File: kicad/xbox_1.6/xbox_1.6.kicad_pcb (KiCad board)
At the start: 4 copper layers, 210 parts, among them J1G1 jst_phd_12, J7G1 jst_phd_12, J8C1 IDC_40_Pin, Q3F1 SOT-23, U2C1 intel_495_bga2, U4B1 ddr_100_tqfp, U4C1 nvidia_xgpu_nv2a, U5F1 ddr_100_tqfp, U6D1 ddr_100_tqfp, U6E1 nvidia_mcpx

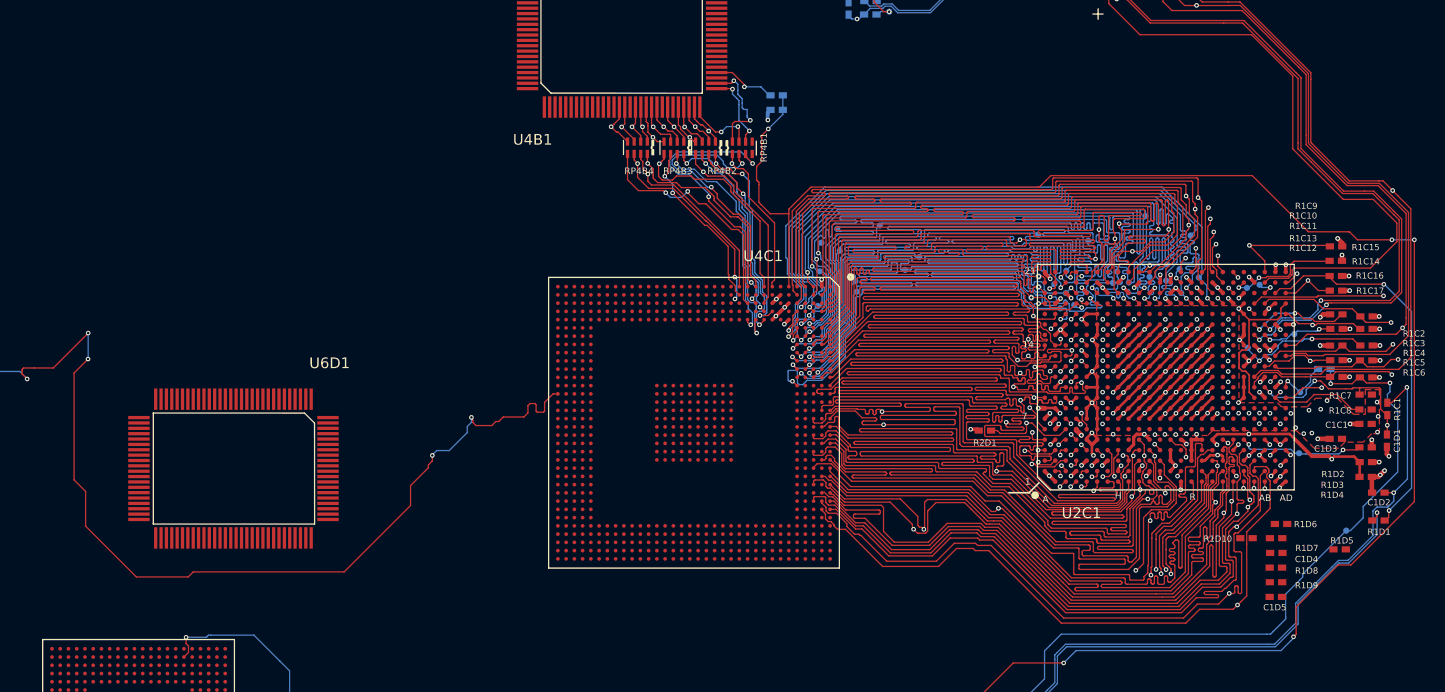
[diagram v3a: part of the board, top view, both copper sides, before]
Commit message: route more cpu signals
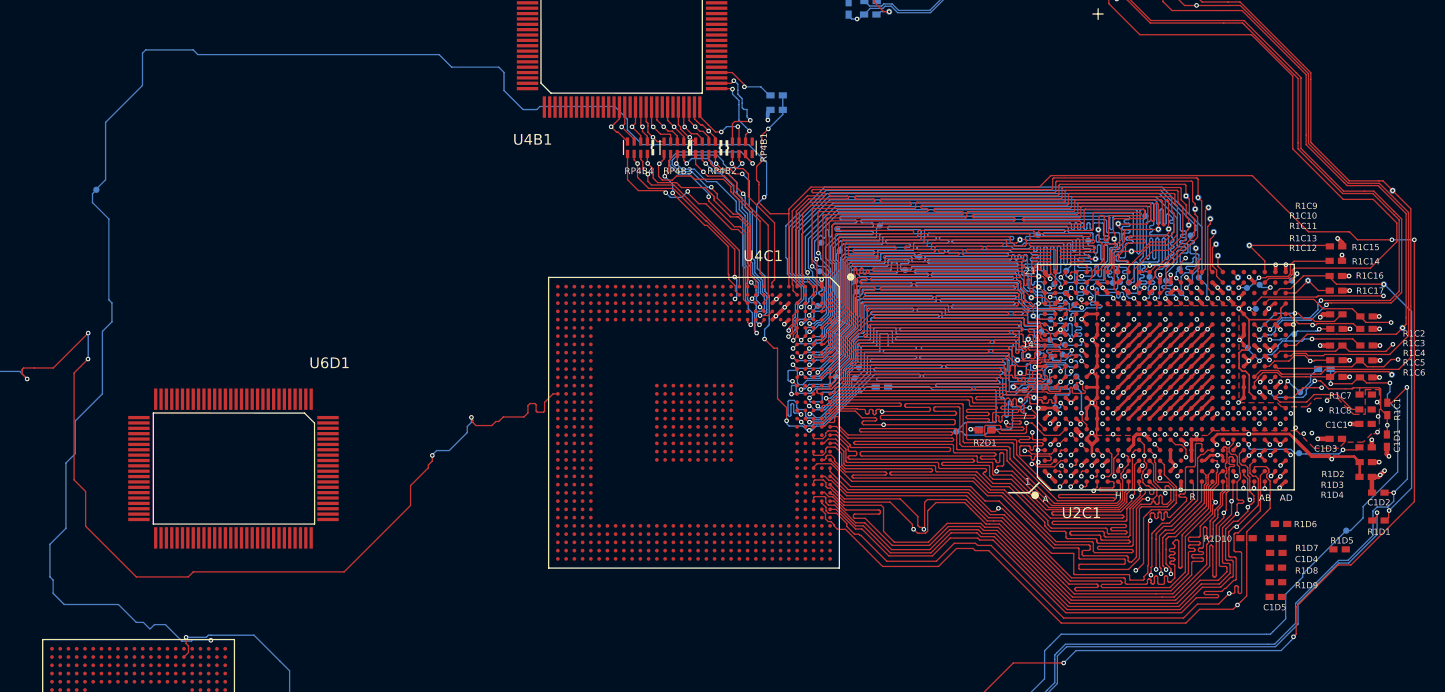
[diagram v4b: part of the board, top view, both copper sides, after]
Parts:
- added C2R8: 0603_smd, xbox_footprint:0603_smd, B.Cu at (253.3, 123.1)
- added R3P1: 0603_smd, xbox_footprint:0603_smd, B.Cu at (240.8, 118.0)
- added REF**: TP, xbox_footprint:TP, B.Cu at (301.6, 105.5)
- added REF**: TP, xbox_footprint:TP, B.Cu at (281.5, 102.1)
- added REF**: TP, xbox_footprint:TP, B.Cu at (278.8, 96.4)
- added REF**: TP, xbox_footprint:TP, B.Cu at (261.1, 117.3)
- added REF**: TP, xbox_footprint:TP, B.Cu at (274.3, 98.9)
- added REF**: TP, xbox_footprint:TP, B.Cu at (286.1, 108.5)
- added REF**: TP, xbox_footprint:TP, B.Cu at (280.6, 97.6)
- added REF**: TP, xbox_footprint:TP, B.Cu at (257.6, 116.3)
- added REF**: TP, xbox_footprint:TP, B.Cu at (285.3, 100.8)
- added REF**: TP, xbox_footprint:TP, B.Cu at (278.8, 101.2)
- added REF**: TP, xbox_footprint:TP, B.Cu at (284.0, 104.7)
- added REF**: TP, xbox_footprint:TP, B.Cu at (262.7, 114.0)
- added REF**: TP, xbox_footprint:TP, B.Cu at (302.6, 116.5)
- added REF**: TP, xbox_footprint:TP, B.Cu at (277.7, 94.8)
- added REF**: TP, xbox_footprint:TP, B.Cu at (257.5, 100.1)
- added REF**: TP, xbox_footprint:TP, B.Cu at (258.5, 112.2)
- added REF**: TP, xbox_footprint:TP, B.Cu at (290.5, 105.1)
- added REF**: TP, xbox_footprint:TP, B.Cu at (268.9, 100.0)
- added REF**: TP, xbox_footprint:TP, B.Cu at (261.8, 120.5)
- added REF**: TP, xbox_footprint:TP, B.Cu at (257.6, 119.6)
- added REF**: TP, xbox_footprint:TP, B.Cu at (257.2, 114.7)
- added REF**: TP, xbox_footprint:TP, B.Cu at (259.8, 113.9)
- added REF**: TP, xbox_footprint:TP, B.Cu at (278.0, 98.4)
- added REF**: TP, xbox_footprint:TP, B.Cu at (303.9, 110.8)
- added REF**: TP, xbox_footprint:TP, B.Cu at (280.4, 96.2)
- added REF**: TP, xbox_footprint:TP, B.Cu at (238.0, 115.6)
- added REF**: TP, xbox_footprint:TP, B.Cu at (260.1, 111.3)
- added REF**: TP, xbox_footprint:TP, B.Cu at (259.1, 109.4)
- added REF**: TP, xbox_footprint:TP, B.Cu at (264.3, 118.0)
- added REF**: TP, xbox_footprint:TP, B.Cu at (261.2, 109.8)
- added REF**: TP, xbox_footprint:TP, B.Cu at (237.5, 116.9)
- added REF**: TP, xbox_footprint:TP, B.Cu at (261.4, 114.3)
- added REF**: TP, xbox_footprint:TP, B.Cu at (249.8, 123.4)
- added REF**: TP, xbox_footprint:TP, B.Cu at (263.0, 112.9)
- added REF**: TP, xbox_footprint:TP, B.Cu at (275.6, 98.8)
- added REF**: TP, xbox_footprint:TP, B.Cu at (281.3, 100.7)
- added REF**: TP, xbox_footprint:TP, B.Cu at (258.5, 114.2)
- added REF**: TP, xbox_footprint:TP, B.Cu at (292.4, 105.1)
- added REF**: TP, xbox_footprint:TP, B.Cu at (258.1, 118.4)
- added REF**: TP, xbox_footprint:TP, B.Cu at (266.7, 102.5)
- added REF**: TP, xbox_footprint:TP, B.Cu at (279.1, 95.0)
- added REF**: TP, xbox_footprint:TP, B.Cu at (271.1, 101.5)
- added REF**: TP, xbox_footprint:TP, B.Cu at (145.6, 94.1)
- added REF**: TP, xbox_footprint:TP, B.Cu at (269.4, 98.2)
- added REF**: TP, xbox_footprint:TP, B.Cu at (259.2, 119.3)
- added REF**: TP, xbox_footprint:TP, B.Cu at (261.2, 112.3)
- added REF**: TP, xbox_footprint:TP, B.Cu at (281.0, 99.2)
- added REF**: TP, xbox_footprint:TP, B.Cu at (282.8, 106.0)
- added REF**: TP, xbox_footprint:TP, B.Cu at (235.2, 116.7)
- added REF**: TP, xbox_footprint:TP, B.Cu at (267.0, 98.9)
- added REF**: TP, xbox_footprint:TP, B.Cu at (302.7, 94.2)
- added REF**: TP, xbox_footprint:TP, B.Cu at (264.4, 116.7)
- added REF**: TP, xbox_footprint:TP, B.Cu at (256.7, 118.0)
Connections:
- U4C1 pad A15: (no net) -> /CPU_D12
- U4C1 pad C13: (no net) -> /CPU_D13
- U4C1 pad C14: (no net) -> /CPU_D19
- U4C1 pad C15: (no net) -> /CPU_D15
- U4C1 pad C16: (no net) -> /CPU_D8
- U4C1 pad C18: (no net) -> /CPU_RESET_R
- U4C1 pad D13: (no net) -> /CPU_D25
- U4C1 pad D15: (no net) -> /CPU_D17
- U4C1 pad D17: (no net) -> /CPU_D1
- U4C1 pad E14: (no net) -> /CPU_D16
- U4C1 pad E16: (no net) -> /CPU_D11
- U4C1 pad E17: (no net) -> /CPU_D3
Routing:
- net /CPU_RESET_R: track 0.00 -> 226.5 mm, vias 0 -> 5
- net /CPU_D15: track 0.87 -> 76.3 mm, vias 1 -> 2
- net /CPU_D11: track 0.87 -> 76.3 mm, vias 1 -> 2
- net /CPU_D16: track 0.88 -> 76.1 mm, vias 1 -> 2
- net /CPU_D19: track 0.90 -> 76.1 mm, vias 1 -> 2
- net /CPU_D3: track 0.89 -> 76.0 mm, vias 1 -> 2
- net /CPU_D13: track 0.75 -> 75.9 mm, vias 1 -> 2
- net /CPU_D1: track 0.88 -> 75.9 mm, vias 1 -> 2
- net /CPU_D25: track 0.90 -> 75.9 mm, vias 1 -> 2
- net /CPU_D8: track 0.88 -> 75.9 mm, vias 1 -> 2
- net /CPU_D12: track 0.91 -> 75.9 mm, vias 1 -> 2
- net /CPU_D17: track 0.86 -> 75.7 mm, vias 1 -> 2
- net /CPU_RESET: track 3.37 -> 37.4 mm
- net /CPU_BERR: track 2.22 -> 5.67 mm
- net /CPU_D18: track 79.8 -> 81.1 mm
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
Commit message: route more CPU signals
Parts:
- added R3B2: 0603_smd, xbox_footprint:0603_smd, F.Cu at (227.4, 94.4)
- added REF**: TP, xbox_footprint:TP, B.Cu at (255.9, 122.3)
- added REF**: TP, xbox_footprint:TP, B.Cu at (244.1, 122.6)
- added REF**: TP, xbox_footprint:TP, B.Cu at (264.0, 121.4)
- added REF**: TP, xbox_footprint:TP, B.Cu at (258.3, 122.4)
- added REF**: TP, xbox_footprint:TP, B.Cu at (259.0, 123.5)
- added REF**: TP, xbox_footprint:TP, B.Cu at (230.0, 124.2)
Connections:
- U4C1 pad D19: (no net) -> /CPU_A15
- U4C1 pad E18: (no net) -> /CPU_D2
- U4C1 pad E19: (no net) -> /CPU_A24
- U6E1 pad AB1: (no net) -> /CPU_RESET_R
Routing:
- net /CPU_A15: track 0.92 -> 76.9 mm, vias 1 -> 2
- net /CPU_D2: track 0.88 -> 76.6 mm, vias 1 -> 2
- net /CPU_A24: track 0.89 -> 76.3 mm, vias 1 -> 2
- net /CPU_RESET_R: track 226.5 -> 230.1 mm

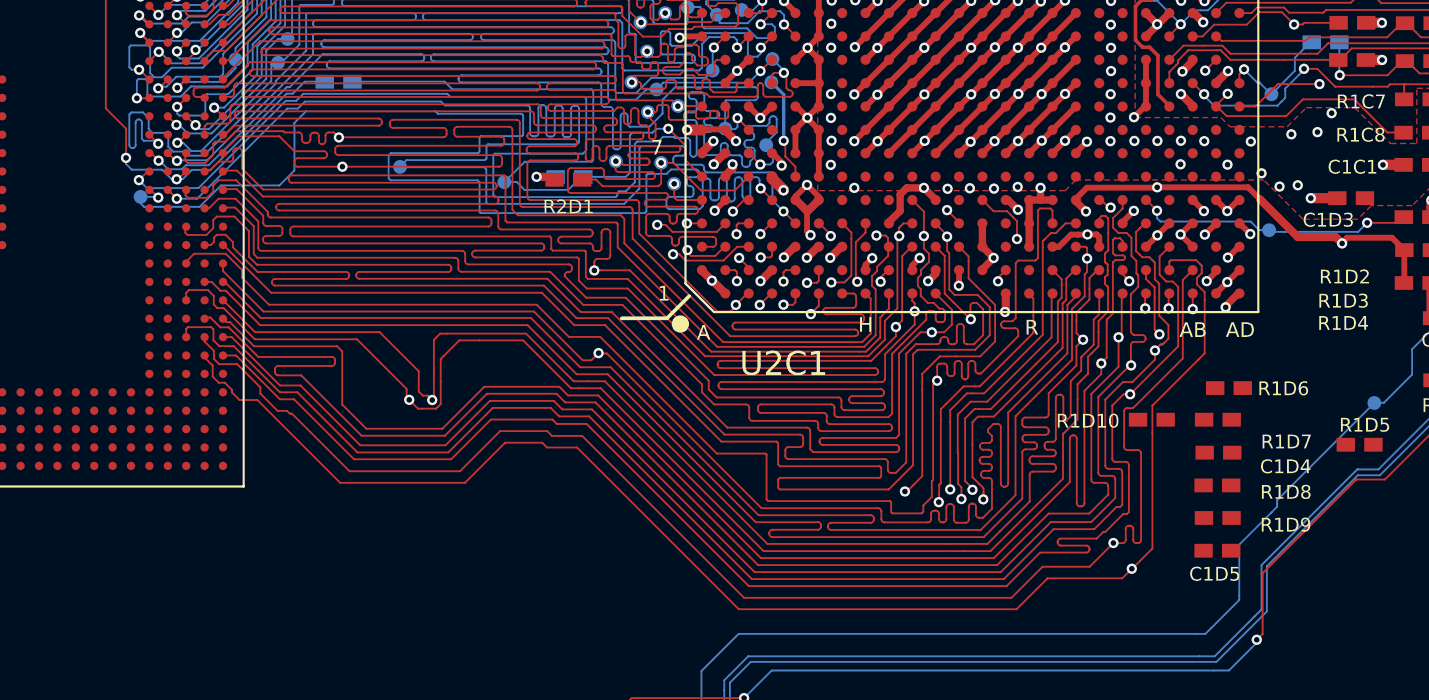
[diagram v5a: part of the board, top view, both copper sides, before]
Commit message: route more CPU traces
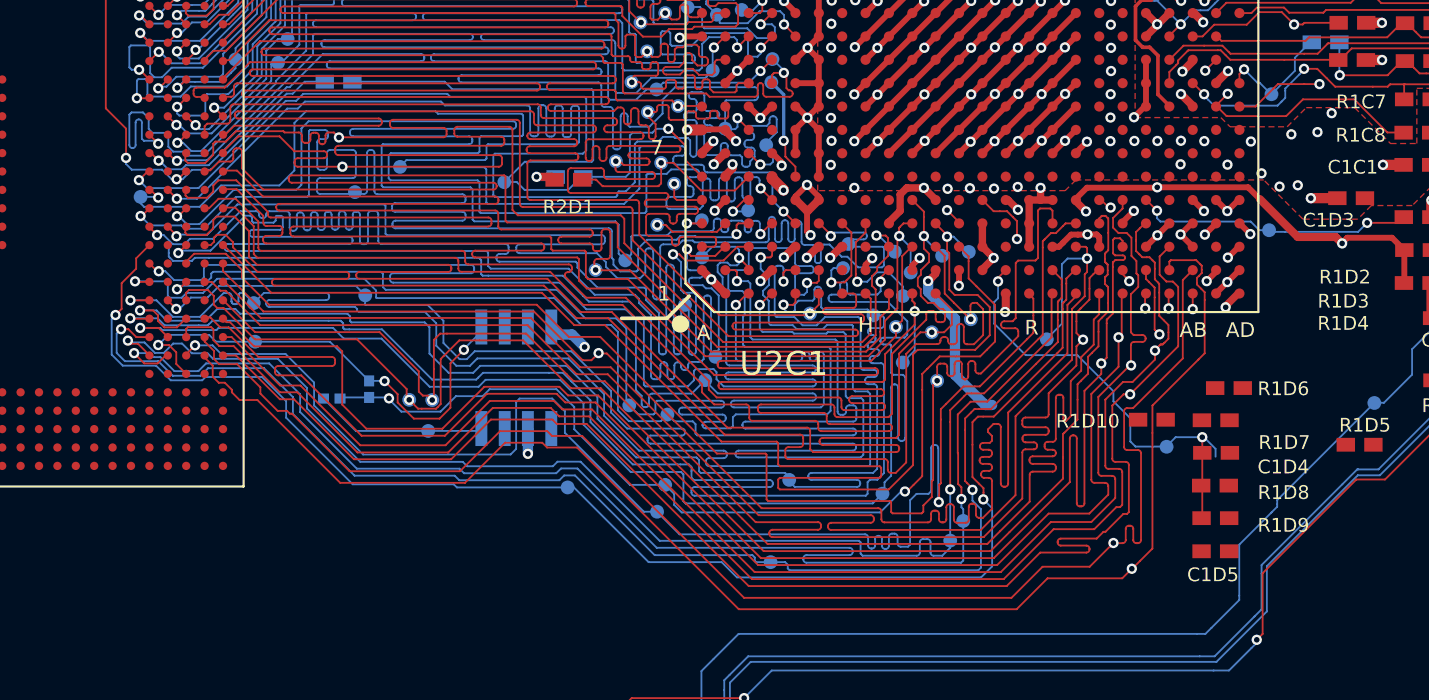
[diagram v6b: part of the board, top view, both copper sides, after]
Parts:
- added R3R1: 0402_smd, xbox_footprint:0402_smd, B.Cu at (242.4, 134.7)
- added R3R2: 0402_smd, xbox_footprint:0402_smd, B.Cu at (240.4, 135.2)
- added REF**: TP, xbox_footprint:TP, B.Cu at (275.0, 127.2)
- added REF**: TP, xbox_footprint:TP, B.Cu at (254.8, 128.2)
- added REF**: TP, xbox_footprint:TP, B.Cu at (258.5, 139.9)
- added REF**: TP, xbox_footprint:TP, B.Cu at (236.2, 132.1)
- added REF**: TP, xbox_footprint:TP, B.Cu at (263.1, 124.9)
- added REF**: TP, xbox_footprint:TP, B.Cu at (258.1, 141.3)
- added REF**: TP, xbox_footprint:TP, B.Cu at (253.2, 140.0)
- added REF**: TP, xbox_footprint:TP, B.Cu at (269.9, 130.7)
- added REF**: TP, xbox_footprint:TP, B.Cu at (271.5, 129.6)
- added REF**: TP, xbox_footprint:TP, B.Cu at (275.1, 130.9)
- added REF**: TP, xbox_footprint:TP, B.Cu at (274.0, 142.9)
- added REF**: TP, xbox_footprint:TP, B.Cu at (271.9, 128.3)
- added REF**: TP, xbox_footprint:TP, B.Cu at (258.7, 136.0)
- added REF**: TP, xbox_footprint:TP, B.Cu at (266.4, 130.6)
- added REF**: TP, xbox_footprint:TP, B.Cu at (270.4, 140.3)
- added REF**: TP, xbox_footprint:TP, B.Cu at (258.1, 125.7)
- added REF**: TP, xbox_footprint:TP, B.Cu at (245.7, 136.9)
- added REF**: TP, xbox_footprint:TP, B.Cu at (244.6, 135.2)
- added REF**: TP, xbox_footprint:TP, B.Cu at (256.4, 127.7)
- added REF**: TP, xbox_footprint:TP, B.Cu at (273.3, 134.2)
- added REF**: TP, xbox_footprint:TP, B.Cu at (271.1, 131.3)
- added REF**: TP, xbox_footprint:TP, B.Cu at (268.5, 126.8)
- added REF**: TP, xbox_footprint:TP, B.Cu at (260.7, 134.2)
- added REF**: TP, xbox_footprint:TP, B.Cu at (260.5, 125.5)
- added REF**: TP, xbox_footprint:TP, B.Cu at (273.6, 127.4)
- added REF**: TP, xbox_footprint:TP, B.Cu at (271.4, 133.2)
- added REF**: TP, xbox_footprint:TP, B.Cu at (274.7, 141.8)
- added REF**: TP, xbox_footprint:TP, B.Cu at (264.3, 144.1)
- added REF**: TP, xbox_footprint:TP, B.Cu at (265.3, 139.6)
- added REF**: TP, xbox_footprint:TP, B.Cu at (245.9, 135.2)
- added REF**: TP, xbox_footprint:TP, B.Cu at (285.8, 137.8)
- added REF**: TP, xbox_footprint:TP, B.Cu at (242.2, 129.6)
- added REF**: TP, xbox_footprint:TP, B.Cu at (268.2, 128.1)
- added REF**: TP, xbox_footprint:TP, B.Cu at (273.0, 131.6)
- added REF**: TP, xbox_footprint:TP, B.Cu at (279.3, 131.9)
- added REF**: TP, xbox_footprint:TP, B.Cu at (259.6, 130.1)
- added REF**: TP, xbox_footprint:TP, B.Cu at (236.2, 130.0)
- added REF**: TP, xbox_footprint:TP, B.Cu at (260.5, 127.5)
- added REF**: TP, xbox_footprint:TP, B.Cu at (271.0, 127.2)
- added REF**: TP, xbox_footprint:TP, B.Cu at (256.6, 135.5)
- added REF**: TP, xbox_footprint:TP, B.Cu at (241.7, 124.0)
- added REF**: TP, xbox_footprint:TP, B.Cu at (261.3, 132.9)
- added U3R1: SOIC8, xbox_footprint:SOIC8, B.Cu at (250.4, 134.0)
- moved R1D8 0.13 mm to (288.4, 139.9)
- moved C1D4 0.13 mm to (288.5, 138.1)
- moved R1D9 0.13 mm to (288.4, 141.7)
- moved R1D7 0.12 mm to (288.5, 136.3)
- moved C1D5 0.11 mm to (288.4, 143.5)
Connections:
- C1D4 pad 1: (no net) -> /CPU_CLKREF
- C1D4 pad 2: (no net) -> /VSS
- R1D8 pad 1: (no net) -> /CPU_CLKREF
- R1D8 pad 2: (no net) -> /VSS
- R1D9 pad 1: (no net) -> /CPU_CLKREF
- U4C1 pad A16: /CPU_A27 -> /CPU_A16
- U4C1 pad C20: (no net) -> /CPU_A25
- U4C1 pad C22: (no net) -> /CPU_A28
- U4C1 pad C24: (no net) -> /CPU_A18
- U4C1 pad C26: (no net) -> /CPU_A23
- U4C1 pad C28: (no net) -> /CPU_LOCK
- U4C1 pad C29: (no net) -> /CPU_BCLK_R
- U4C1 pad D21: (no net) -> /CPU_A17
- U4C1 pad D25: (no net) -> /CPU_A22
- U4C1 pad D27: (no net) -> /CPU_A5
- U4C1 pad D28: (no net) -> /CPU_DRDY
- U4C1 pad E20: (no net) -> /CPU_A20
- U4C1 pad E21: (no net) -> /CPU_A26
- U4C1 pad E22: (no net) -> /CPU_TRDY
- U4C1 pad E23: (no net) -> /CPU_A27
- U4C1 pad E24: (no net) -> /CPU_A30
- U4C1 pad E25: (no net) -> /CPU_A21
- U4C1 pad E26: (no net) -> /CPU_A19
- U4C1 pad E27: (no net) -> /CPU_REQ0
- U4C1 pad E28: (no net) -> /CPU_BPRI
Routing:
- net /CPU_A19: track 1.19 -> 78.0 mm, vias 1 -> 2
- net /CPU_A5: track 0.85 -> 77.0 mm, vias 1 -> 2
- net /CPU_A21: track 1.14 -> 77.0 mm, vias 1 -> 2
- net /CPU_A25: track 0.87 -> 76.4 mm, vias 1 -> 2
- net /CPU_A22: track 0.93 -> 76.4 mm, vias 1 -> 2
- net /CPU_A23: track 1.20 -> 76.6 mm, vias 1 -> 2
- net /CPU_A18: track 1.27 -> 76.6 mm, vias 1 -> 2
- net /CPU_A30: track 1.17 -> 76.5 mm, vias 1 -> 2
- net /CPU_A17: track 0.98 -> 75.6 mm, vias 1 -> 2
- net /CPU_A16: track 1.30 -> 75.7 mm
- net /CPU_A28: track 2.47 -> 75.8 mm, vias 1 -> 2
- net /CPU_A20: track 1.20 -> 74.2 mm, vias 1 -> 2
- net /CPU_A26: track 4.56 -> 75.5 mm, vias 1 -> 2
- net /CPU_A31: track 0.88 -> 69.0 mm
- net /CPU_TRDY: track 15.6 -> 80.0 mm, vias 1 -> 2
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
